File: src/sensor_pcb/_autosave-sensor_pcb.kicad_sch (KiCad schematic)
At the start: 19 parts, among them IC1 TCAN3414DRBR, J1 662004231722, J2 643280100305, J3 66200821022, J4 66200821022, J5 662004231722, J6 643280100305, U1 SHT45-AD1B, U2 16-bit ADC, U4 BMP581

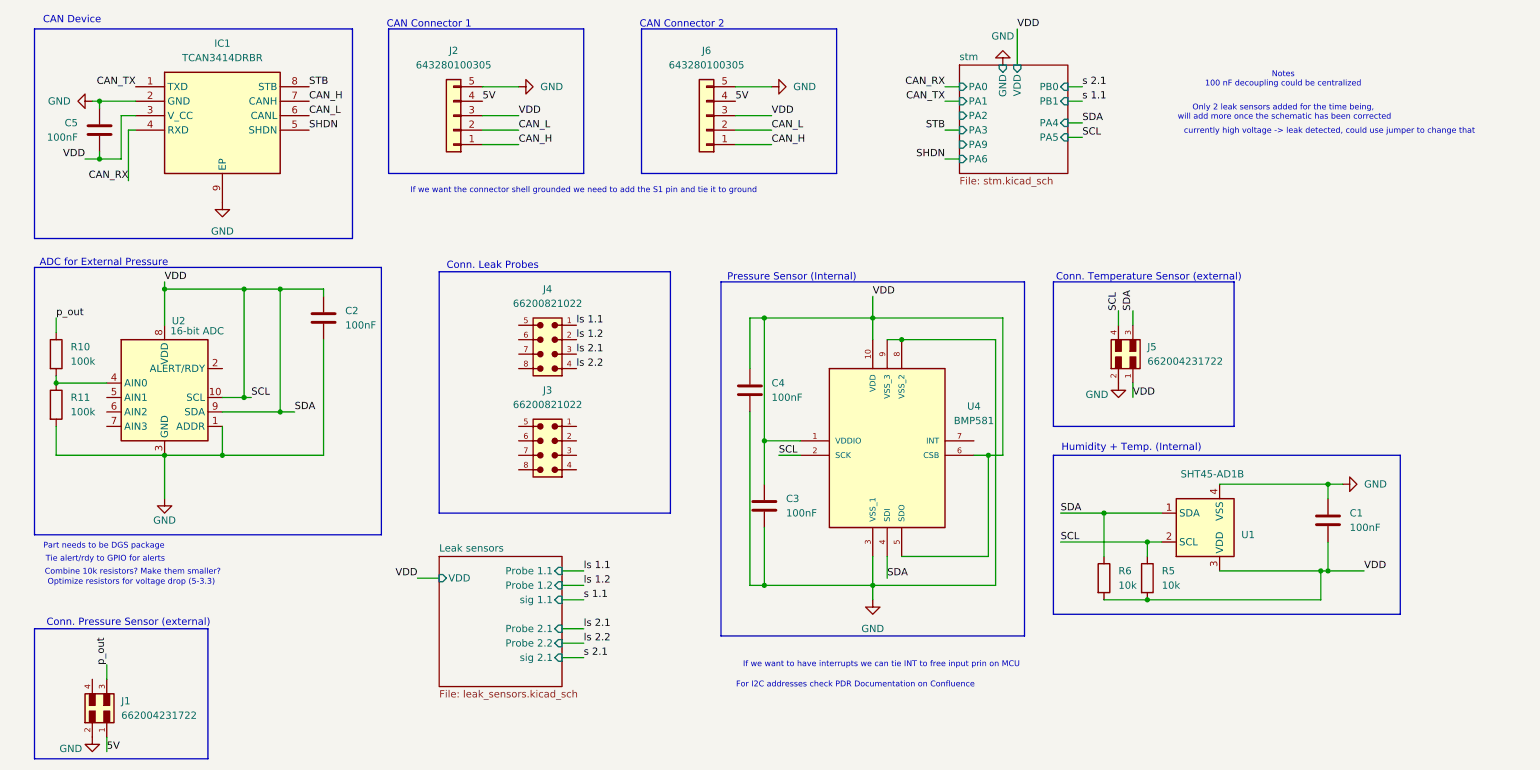
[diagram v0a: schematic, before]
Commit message: schematic update
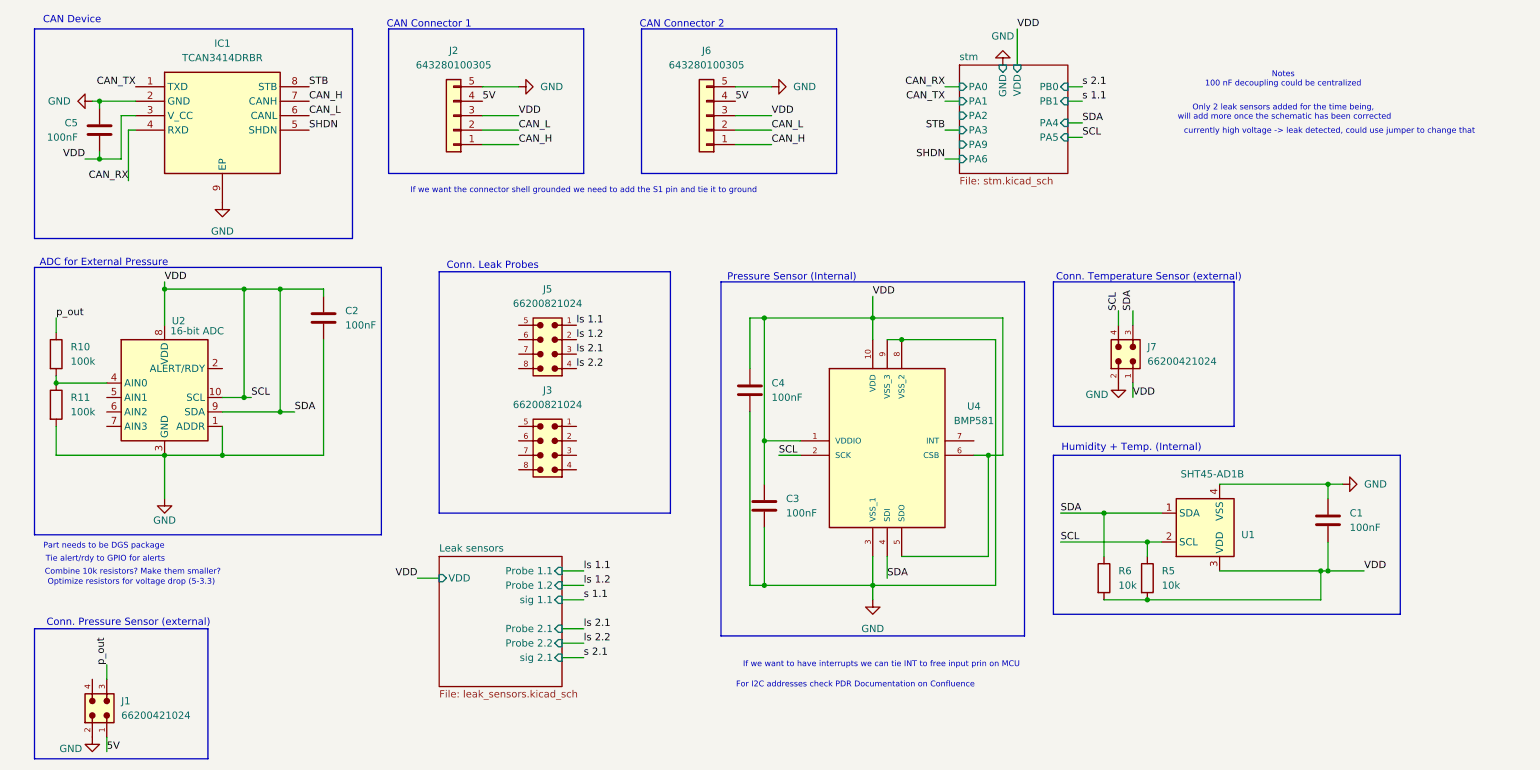
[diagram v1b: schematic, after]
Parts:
- removed J1, J5: 662004231722, dz_con:Wurth_662004231722, symbol #dzdb:s_con/CON-WUR-662004231722
- removed J3, J4: 66200821022, dz_con:Wurth_66200821022, symbol #dzdb:s_con/CON-WUR-66200821022
- added J1, J7: 66200421024, dz_con:Wurth_66200421024, symbol #dzdb:s_con/CON-WUR-66200421024
- added J3, J5: 66200821024, dz_con:Wurth_66200821024, symbol #dzdb:s_con/CON-WUR-66200821024
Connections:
- net 5V: now also J1.1
- net GND: now also J1.2, J7.2
- net SCL: now also J7.1, J7.3, J7.4
- net ls 1.1: now also J5.1
- net ls 1.2: now also J5.2
- net ls 2.1: now also J5.3
- net ls 2.2: now also J5.4
- net p_out: now also J1.3
